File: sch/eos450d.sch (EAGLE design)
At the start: 17 parts, among them IC1 74595

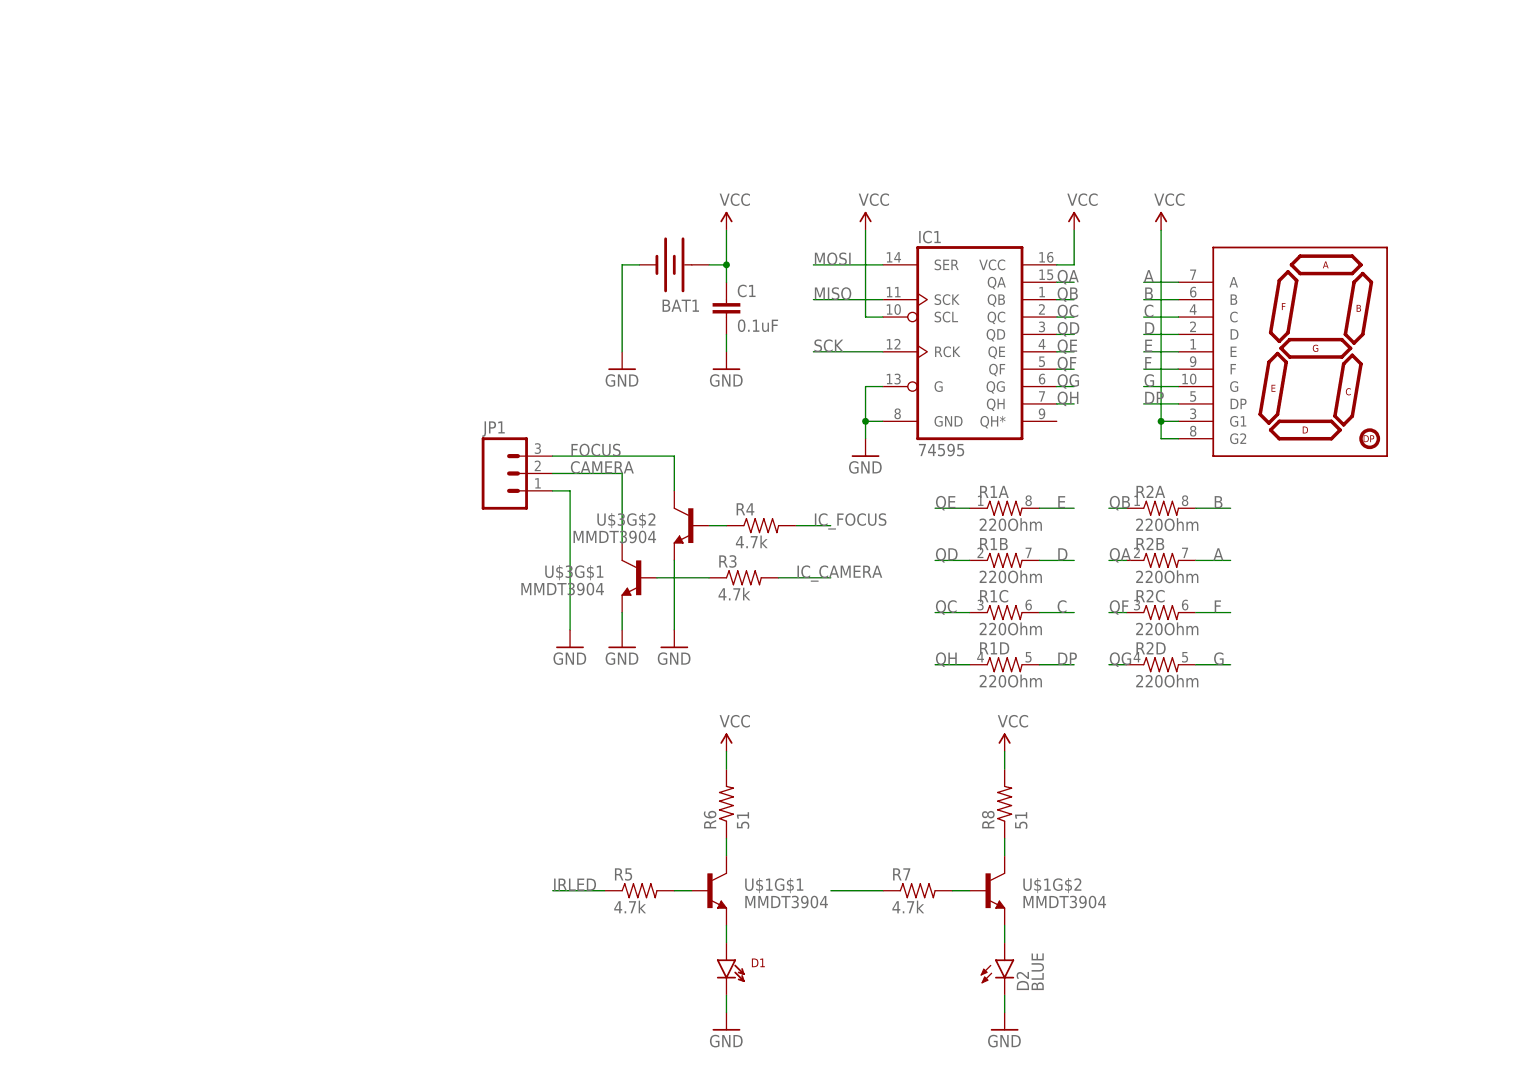
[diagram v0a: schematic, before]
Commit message: Updated schematic. Updated source code: WDT usage
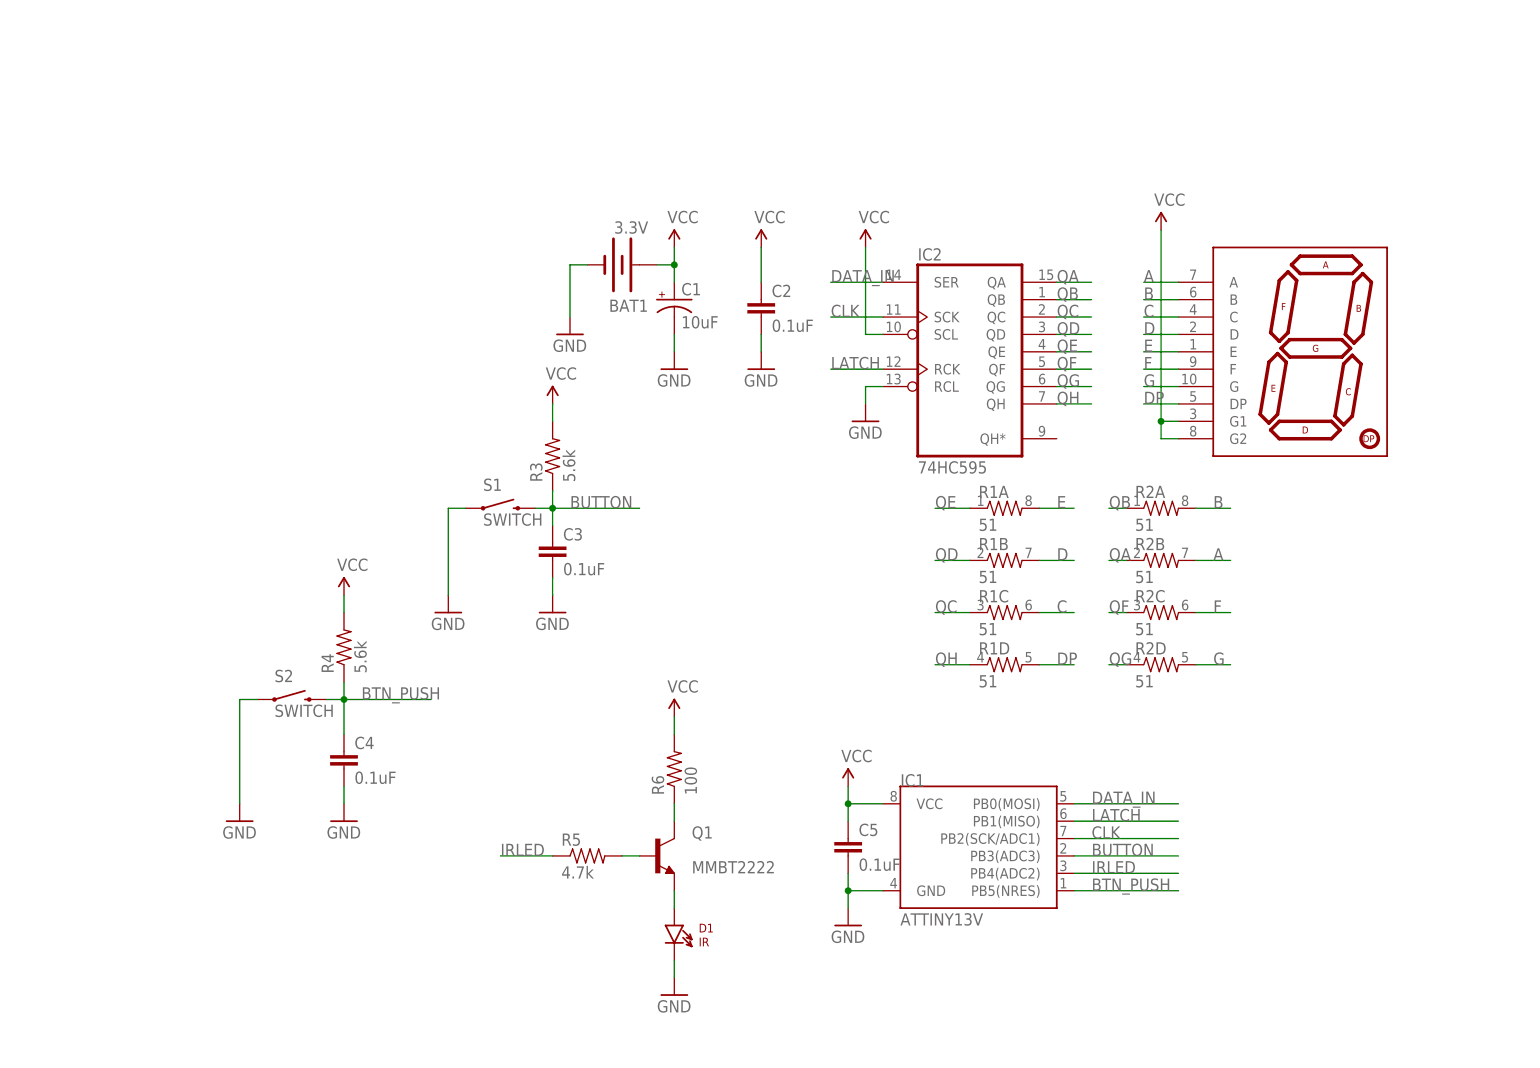
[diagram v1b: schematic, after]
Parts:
- removed JP1: (no value), SparkFun-Connectors:M03PTH
- removed R7: 4.7k, SparkFun-Passives:RESISTOR0805-RES
- removed R8: 51, SparkFun-Passives:RESISTOR0805-RES
- removed U$1, U$3: MMDT3904, SparkFun-DiscreteSemi:MMDT3904
- removed U$2: 7-SEGMENT-DISPLAY-1"-REDEZ, SparkFun-Displays:7-SEGMENT-DISPLAY-1"-REDEZ
- added C2, C3, C4, C5: 0.1uF, SparkFun-Capacitors:0.1UF-25V-5%(0603)
- added IC2: 74HC595, 74xx-us:74LS594D
- added Q1: MMBT2222, transistor-neu-to92:MMBT2222ALT1-NPN-SOT23-BEC
- added S1, S2: SWITCH, SparkFun-Electromechanical:SWITCH-MOMENTARY-2SMD-REDUNDANT
- BAT1: value (none) -> 3.3V
- C1: value 0.1uF -> 10uF; device SparkFun-Capacitors:CAP0805 -> SparkFun-Capacitors:10UF-16V-10%(TANT)
- D1: value (none) -> IR
- D2: value BLUE -> 7-SEGMENT-DISPLAY-1"-REDEZ; device SparkFun-LED:LED-BLUE0603 -> SparkFun-Displays:7-SEGMENT-DISPLAY-1"-REDEZ
- IC1: value 74595 -> ATTINY13V; device SparkFun-DigitalIC:74595 -> SparkFun-DigitalIC:ATTINY13SOIC
- R1, R2: value 220Ohm -> 51
- R3, R4: value 4.7k -> 5.6k
- R6: value 51 -> 100
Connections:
- removed net CAMERA: JP1.2, U$3G$1.C
- removed net FOCUS: JP1.3, U$3G$2.C
- removed net IC_CAMERA: R3.2
- removed net IC_FOCUS: R4.2
- removed net MISO: IC1.SCK
- removed net MOSI: IC1.SER
- removed net N$20: R3.1, U$3G$1.B
- removed net N$21: R4.1, U$3G$2.B
- removed net N$3: R7.2, U$1G$2.B
- removed net N$5: R7.1
- removed net N$6: D2.A, U$1G$2.E
- removed net N$7: R8.1, U$1G$2.C
- removed net SCK: IC1.RCK
- new net BTN_PUSH: C4.1, IC1.PB5(NRES), R4.1, S2.2
- new net BUTTON: C3.1, IC1.PB3(ADC3), R3.1, S1.2
- new net CLK: IC1.PB2(SCK/ADC1), IC2A.SCK
- new net DATA_IN: IC1.PB0(MOSI), IC2A.SER
- new net LATCH: IC1.PB1(MISO), IC2A.RCK
- net A: now also D2.A; no longer U$2.A
- net B: now also D2.B; no longer U$2.B
- net C: now also D2.C; no longer U$2.C
- net D: now also D2.D; no longer U$2.D
- net DP: now also D2.DP; no longer U$2.DP
- net E: now also D2.E; no longer U$2.E
- net F: now also D2.F; no longer U$2.F
- net G: now also D2.G; no longer U$2.G
- net GND: now also C1.-, C2.2, C3.2, C4.2, C5.2, IC2A.RCL, S1.1, S2.1; no longer C1.2, D2.C, IC1.G, JP1.1, U$3G$1.E, U$3G$2.E
- net IRLED: now also IC1.PB4(ADC2)
- net N$1: now also Q1.E; no longer U$1G$1.E
- net N$2: now also Q1.B; no longer U$1G$1.B
- net N$4: now also Q1.C; no longer U$1G$1.C
- net QA: now also IC2A.QA; no longer IC1.QA
- net QB: now also IC2A.QB; no longer IC1.QB
- net QC: now also IC2A.QC; no longer IC1.QC
- net QD: now also IC2A.QD; no longer IC1.QD
- net QE: now also IC2A.QE; no longer IC1.QE
- net QF: now also IC2A.QF; no longer IC1.QF
- net QG: now also IC2A.QG; no longer IC1.QG
- net QH: now also IC2A.QH; no longer IC1.QH
- net VCC: now also C1.+, C2.1, C5.1, D2.G1, D2.G2, IC2A.SCL, R3.2, R4.2; no longer C1.1, IC1.SCL, R8.2, U$2.G1, U$2.G2
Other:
- moved on the sheet: BAT1, D1, R3, R4, R5, R6

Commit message: Schematic complete. Added Gerber files
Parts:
- removed IC1: ATTINY13V, SparkFun-DigitalIC:ATTINY13SOIC
- added ISP1: AVRISP-6, adafruit:AVRISP-6
- added U1: Tiny45-20-SMT, SparkFun-DigitalIC:ATTINY45TINY45-20-SMT
- R1, R2: value 51 -> 330
- R3, R4: value 5.6k -> 10k
- R5: value 4.7k -> 3.3k
- R6: value 100 -> 180
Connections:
- removed net N$4: Q1.C, R6.1
- new net N$3: D1.C, Q1.C
- net BTN_PUSH: now also ISP1.RST, U1.PB5(NRES); no longer IC1.PB5(NRES)
- net BUTTON: now also U1.PB3(ADC3); no longer IC1.PB3(ADC3)
- net CLK: now also ISP1.SCK, U1.PB2(SCK/ADC1); no longer IC1.PB2(SCK/ADC1)
- net DATA_IN: now also ISP1.MOSI, U1.PB0(MOSI); no longer IC1.PB0(MOSI)
- net GND: now also ISP1.GND, Q1.E, U1.GND; no longer D1.C, IC1.GND
- net IRLED: now also U1.PB4(ADC2); no longer IC1.PB4(ADC2)
- net LATCH: now also ISP1.MISO, U1.PB1(MISO); no longer IC1.PB1(MISO)
- net N$1: now also R6.1; no longer Q1.E
- net VCC: now also ISP1.VCC, U1.VCC; no longer IC1.VCC
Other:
- note added: "1.4V 20mA"
- note added: "40mA"
- note added: "R5 = 0.2 × R6 × hFE(Q1)"
- moved on the sheet: D1, R6

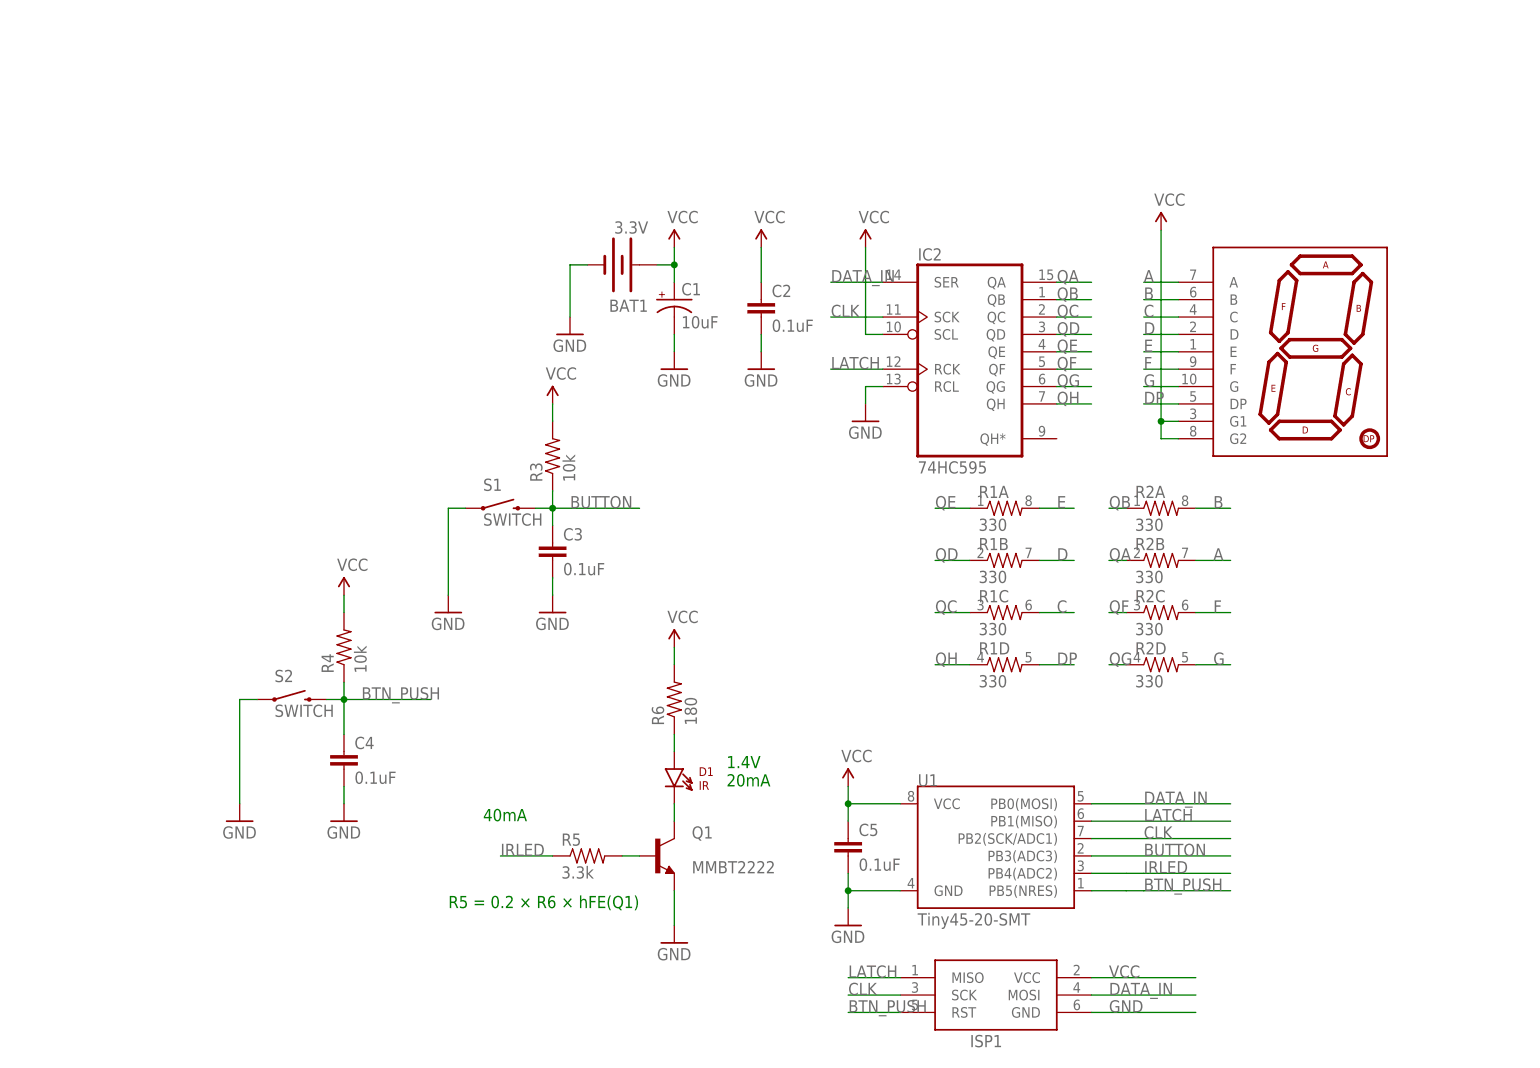
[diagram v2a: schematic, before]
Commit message: Schematic updated: Auto power switching added
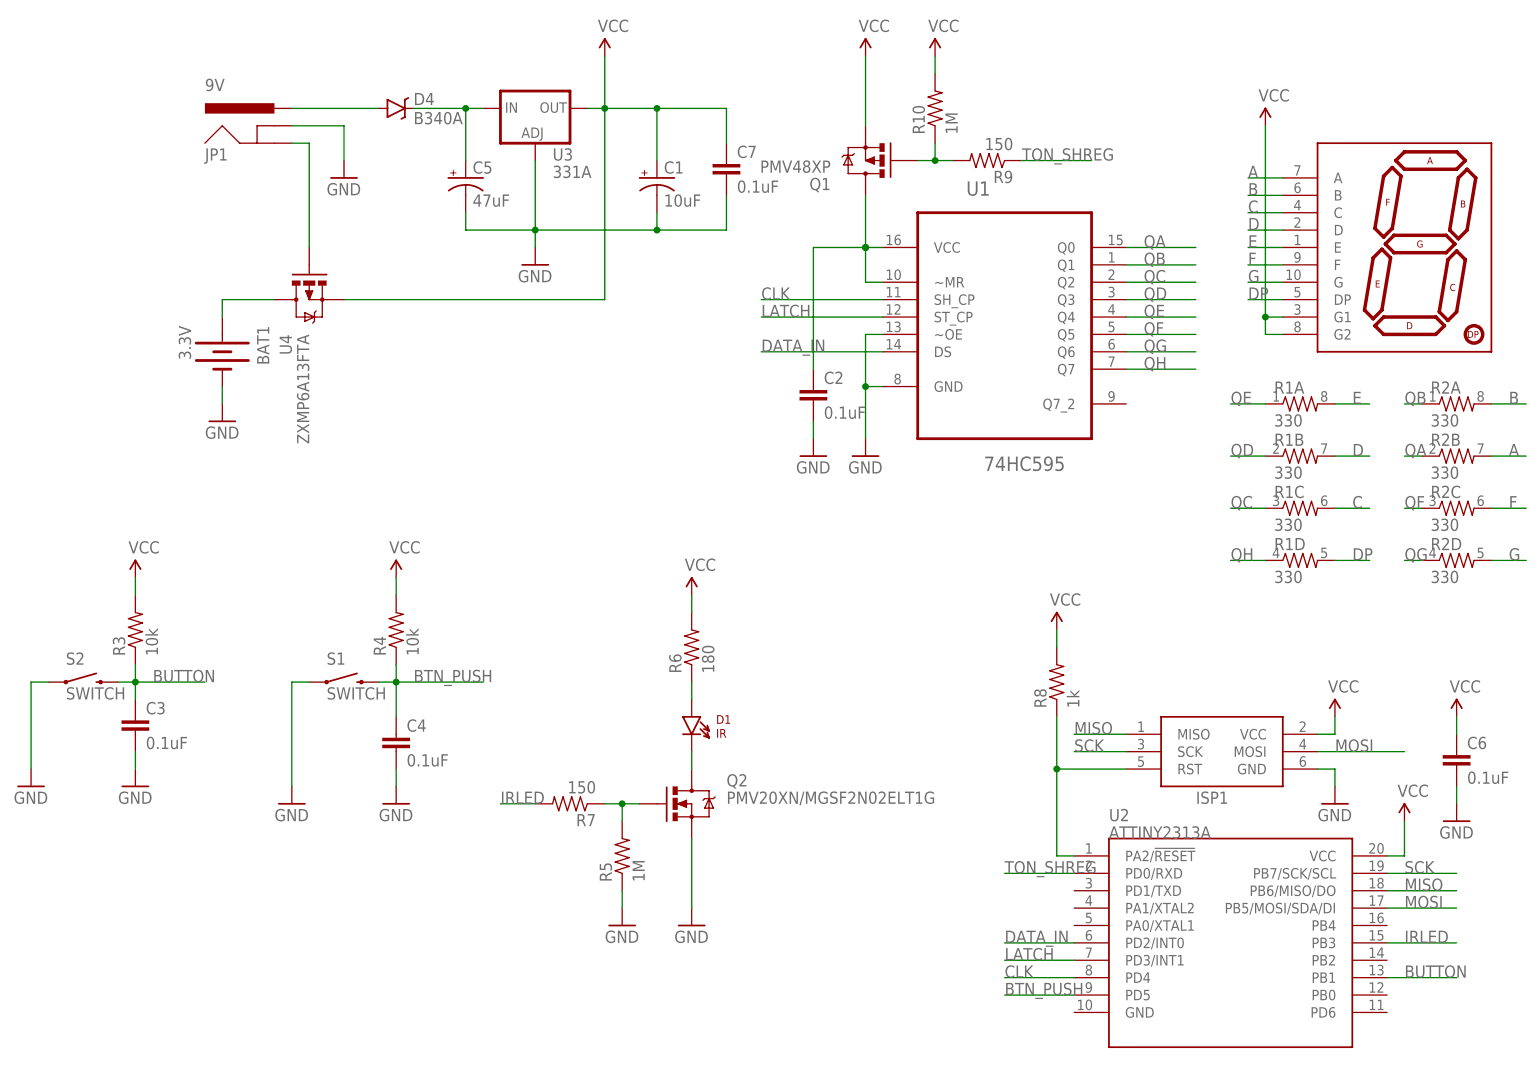
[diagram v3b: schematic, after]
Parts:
- removed IC2: 74HC595, 74xx-us:74LS594D
- added C6, C7: 0.1uF, SparkFun-Capacitors:0.1UF-25V-5%(0603)
- added D4: B340A, SparkFun-DiscreteSemi:DIODE-SCHOTTKY-B340A
- added JP1: 9V, SparkFun-Connectors:POWER_JACKSLT
- added Q2: PMV20XN/MGSF2N02ELT1G, mine-mosfet:PMV20XN
- added R10: 1M, SparkFun-Passives:RESISTOR0805-RES
- added R7, R9: 150, SparkFun-Passives:RESISTOR0805-RES
- added R8: 1k, SparkFun-Passives:RESISTOR0805-RES
- added U2: ATTINY2313A, SparkFun-DigitalIC:ATTINY2313A
- added U3: 331A, SparkFun-PowerIC:V_REG_317SMD
- added U4: ZXMP6A13FTA, mine-mosfet:ZXMP6A13FTA
- C5: value 0.1uF -> 47uF; device SparkFun-Capacitors:0.1UF-25V-5%(0603) -> SparkFun-Capacitors:10UF-20V-10%(TANT)
- Q1: value MMBT2222 -> PMV48XP; device transistor-neu-to92:MMBT2222ALT1-NPN-SOT23-BEC -> mine-mosfet:PMV48XP
- R5: value 3.3k -> 1M
- S1, S2: device SparkFun-Electromechanical:SWITCH-MOMENTARY-2SMD-REDUNDANT -> SparkFun-Electromechanical:SWITCH-MOMENTARY-2PTH_EZ
- U1: value Tiny45-20-SMT -> 74HC595; device SparkFun-DigitalIC:ATTINY45TINY45-20-SMT -> mine-mosfet:74HC595D
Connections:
- new net MISO: ISP1.MISO, U2.PB6/MISO/DO
- new net MOSI: ISP1.MOSI, U2.PB5/MOSI/SDA/DI
- new net N$10: D4.A, JP1.PWR
- new net N$11: BAT1.+, U4.D
- new net N$12: JP1.GND, U4.G
- new net N$4: Q1.G, R10.1, R9.2
- new net N$5: C2.1, Q1.D, U1.VCC, U1.~MR
- new net N$6: C5.+, D4.C, U3.IN
- new net N$7: ISP1.RST, R8.1, U2.PA2/!RESET
- new net SCK: ISP1.SCK, U2.PB7/SCK/SCL
- new net TON_SHREG: R9.1, U2.PD0/RXD
- net BTN_PUSH: now also S1.2, U2.PD5; no longer ISP1.RST, S2.2, U1.PB5(NRES)
- net BUTTON: now also S2.2, U2.PB1; no longer S1.2, U1.PB3(ADC3)
- net CLK: now also U1.SH_CP, U2.PD4; no longer IC2A.SCK, ISP1.SCK, U1.PB2(SCK/ADC1)
- net DATA_IN: now also U1.DS, U2.PD2/INT0; no longer IC2A.SER, ISP1.MOSI, U1.PB0(MOSI)
- net GND: now also C5.-, C6.2, C7.2, JP1.GNDBREAK, Q2.S, R5.1, U1.~OE, U3.ADJ; no longer C5.2, IC2A.RCL, Q1.E
- net IRLED: now also R7.2, U2.PB3; no longer R5.1, U1.PB4(ADC2)
- net LATCH: now also U1.ST_CP, U2.PD3/INT1; no longer IC2A.RCK, ISP1.MISO, U1.PB1(MISO)
- net N$2: now also Q2.G, R7.1; no longer Q1.B
- net N$3: now also Q2.D; no longer Q1.C
- net QA: now also U1.Q0; no longer IC2A.QA
- net QB: now also U1.Q1; no longer IC2A.QB
- net QC: now also U1.Q2; no longer IC2A.QC
- net QD: now also U1.Q3; no longer IC2A.QD
- net QE: now also U1.Q4; no longer IC2A.QE
- net QF: now also U1.Q5; no longer IC2A.QF
- net QG: now also U1.Q6; no longer IC2A.QG
- net QH: now also U1.Q7; no longer IC2A.QH
- net VCC: now also C6.1, C7.1, Q1.S, R10.2, R8.2, U2.VCC, U3.OUT, U4.S; no longer BAT1.+, C2.1, C5.1, IC2A.SCL, U1.VCC
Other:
- note removed: "1.4V 20mA"
- note removed: "40mA"
- note removed: "R5 = 0.2 × R6 × hFE(Q1)"
- moved on the sheet: BAT1, C1, C2, C3, C4, D1, ISP1, R1A, R1B, R1C, R1D, R2A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
